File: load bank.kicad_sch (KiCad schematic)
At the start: 31 parts, among them J1 25SH-B-02-TS, J10 25SH-B-02-TS, J11 EURO_BLOCK,_3_POSITION, J12 EURO_BLOCK,_3_POSITION, J2 LHD-03-TS, J3 EBBA-03-C-SS-BU, J4 25SH-B-02-TS, J5 Conn_01x02_Male, J6 Conn_01x02_Male, J7 696101000002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

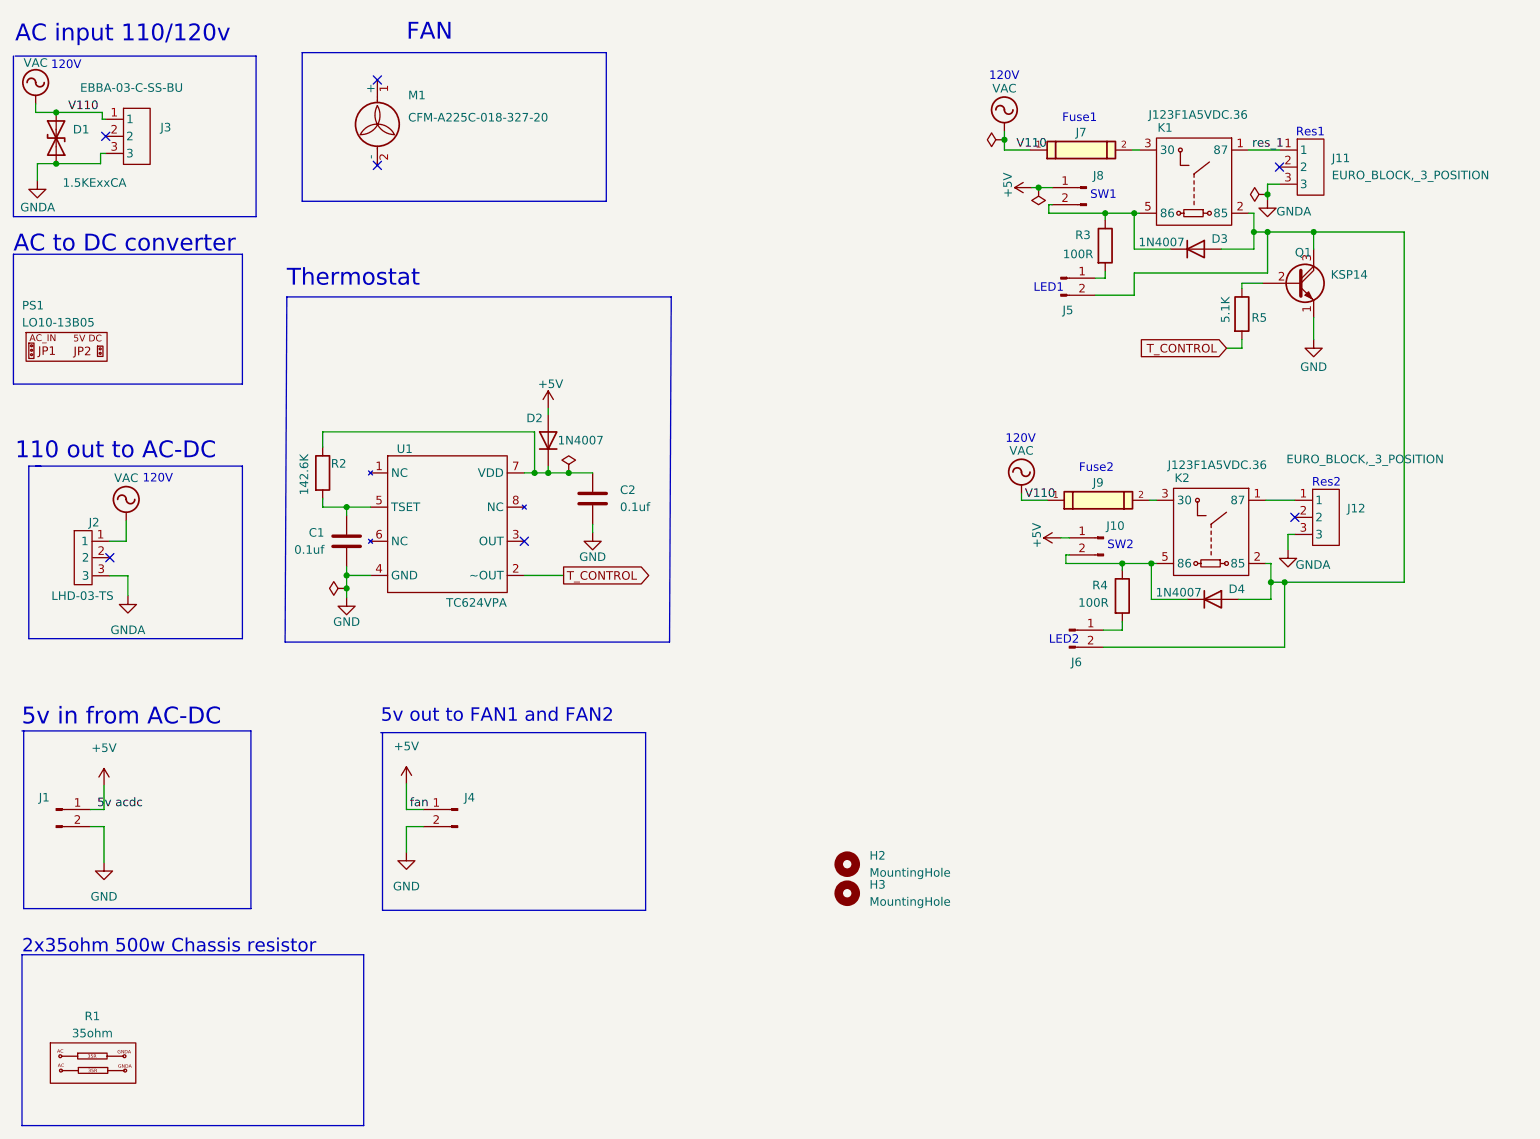
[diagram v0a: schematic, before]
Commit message: added second fan connector for parallel connection
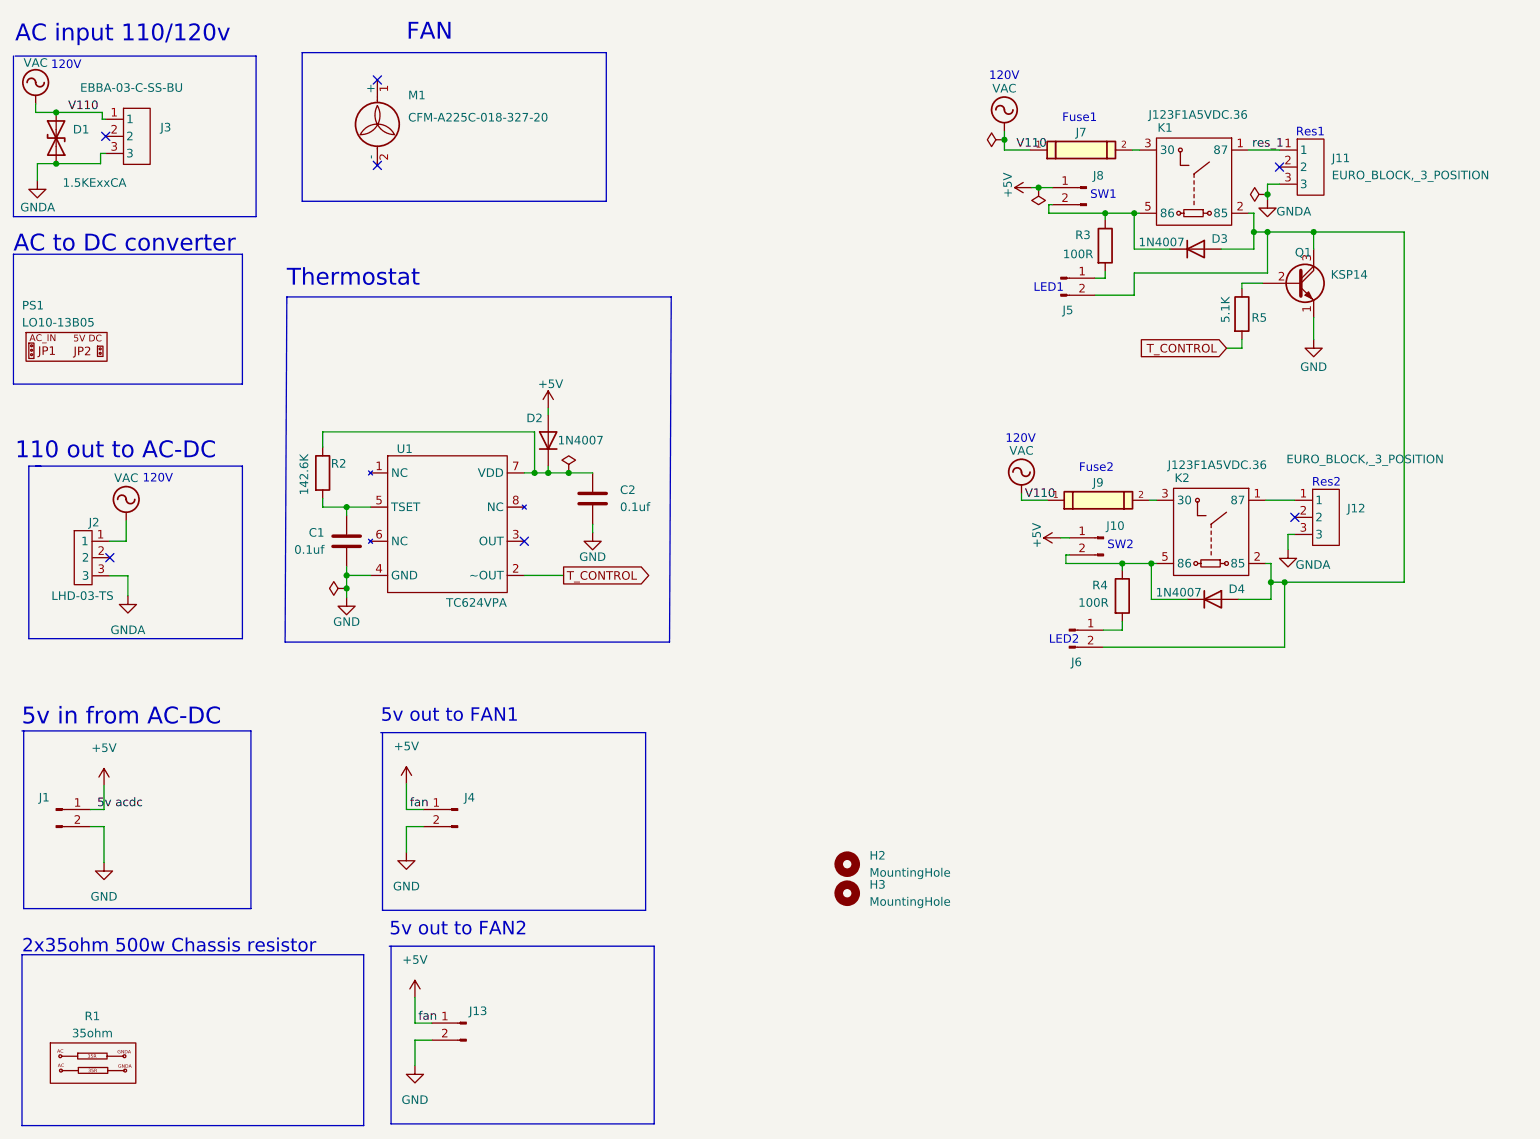
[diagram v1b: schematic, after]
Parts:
- added J13: 25SH-B-02-TS, Connector_JST:JST_EH_B2B-EH-A_1x02_P2.50mm_Vertical, symbol Connector:Conn_01x02_Male
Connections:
- net +5V: now also J13.1 (Pin_1)
- net GND: now also J13.2 (Pin_2)
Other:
- note added: "5v out to FAN1"
- note added: "5v out to FAN2"
- note removed: "5v out to FAN1 and FAN2"

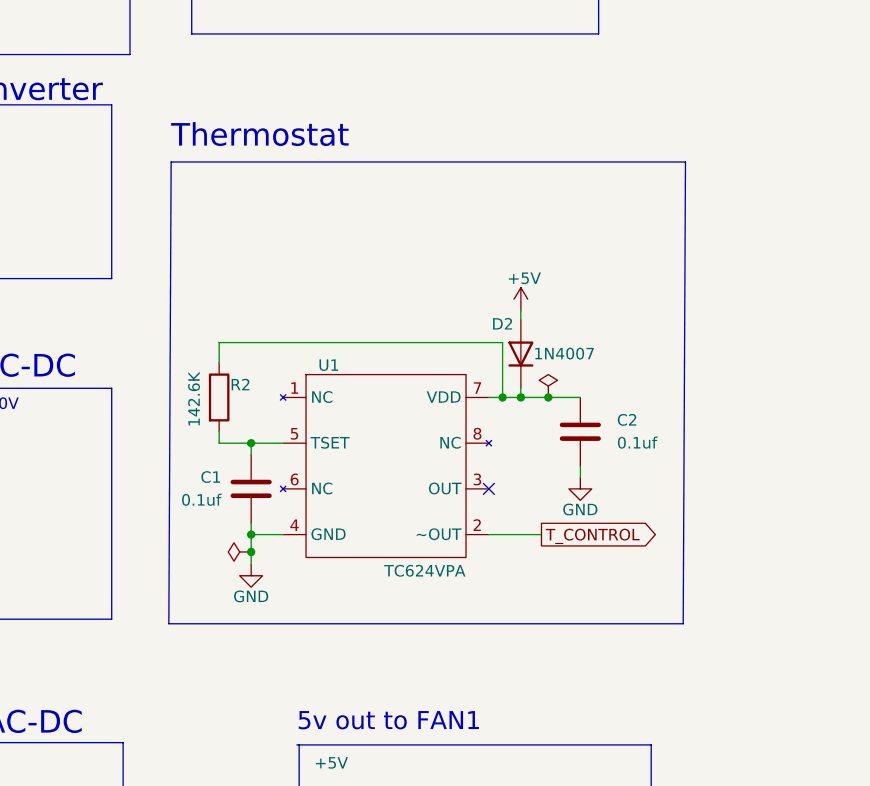
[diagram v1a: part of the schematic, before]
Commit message: added 4.7v zener + resistor to keep TC624 voltage in range
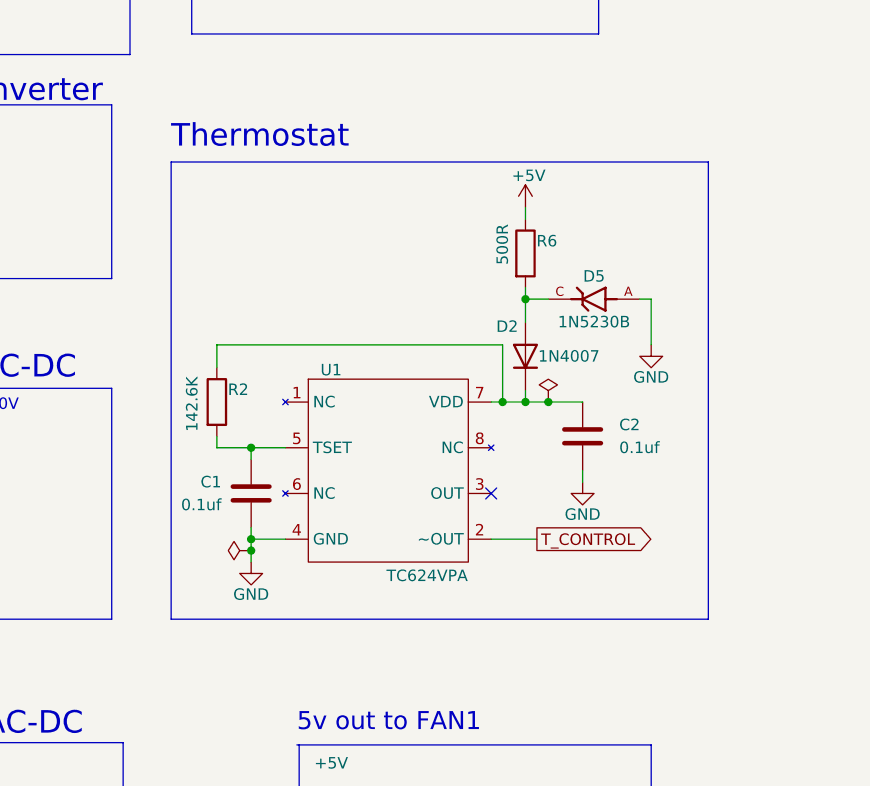
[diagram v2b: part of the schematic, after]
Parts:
- added D5: 1N5230B, DIOAD928W47L399D179, symbol 1N5231B_R0:1N5231B_R0
- added R6: 500R, Resistor_THT:R_Axial_DIN0207_L6.3mm_D2.5mm_P7.62mm_Horizontal, symbol Device:R
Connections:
- net +5V: now also R6.1; no longer D2.2 (A)
- net GND: now also D5.A
- new net: D2.2 (A), D5.C, R6.2
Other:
- moved on the sheet: C1, C2, D2, R2, U1
